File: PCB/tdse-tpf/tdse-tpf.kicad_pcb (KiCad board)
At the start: 2 copper layers, 100 x 100 mm, 11 parts, among them J1 CN7, J2 CN10, J3 Conn_01x04, J4 Conn_01x05, J5 Conn_01x02, J6 Conn_01x16, J7 Conn_01x04

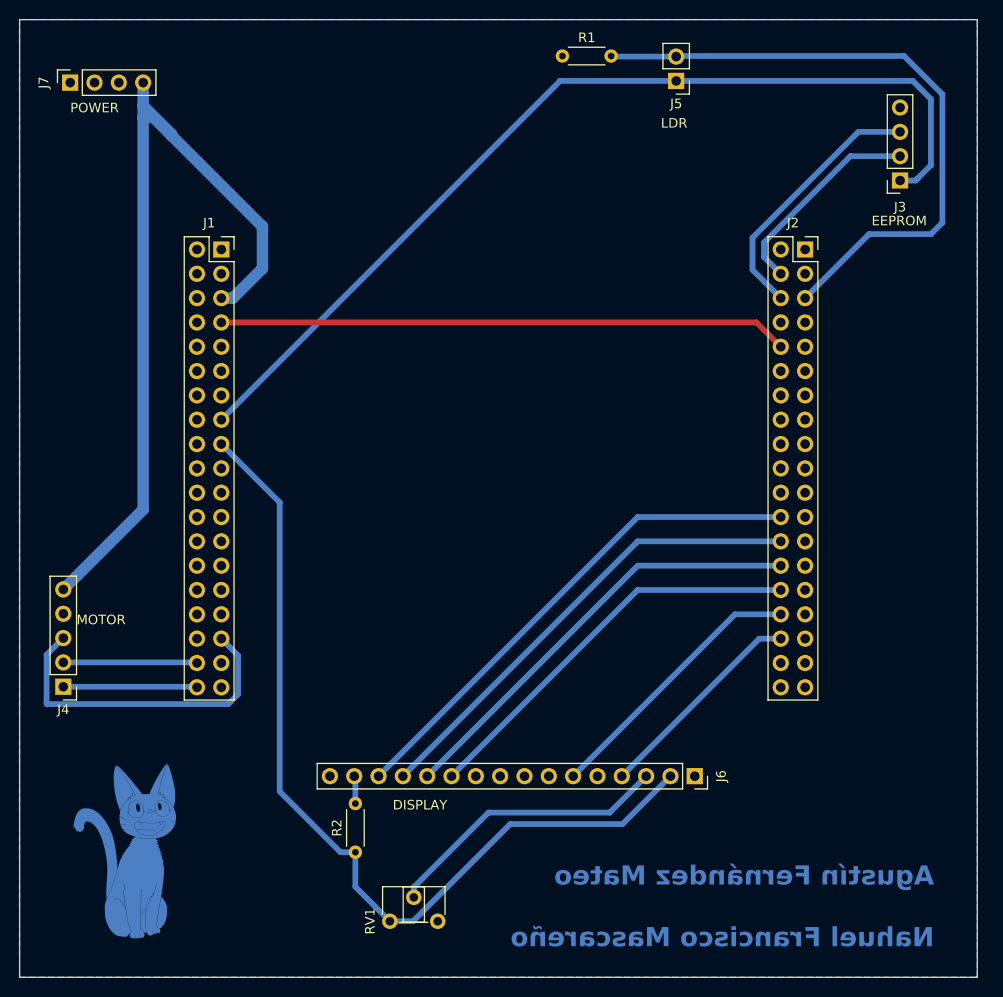
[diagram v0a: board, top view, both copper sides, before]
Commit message: Changed pins sensor-ldr-display & updated pcb pads
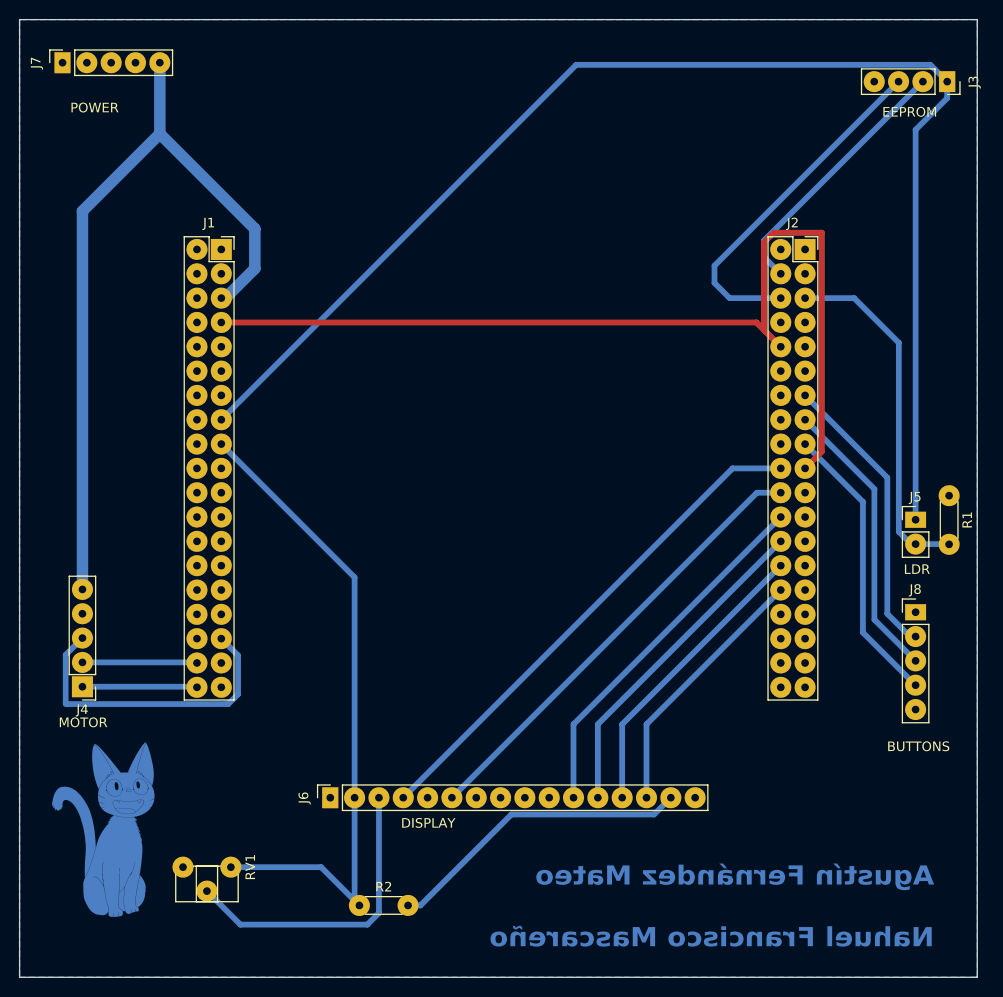
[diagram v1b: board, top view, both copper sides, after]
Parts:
- added J8: Conn_01x05, Connector_PinHeader_2.54mm:PinHeader_1x05_P2.54mm_Vertical, F.Cu at (180.0, 99.9)
- J7: value Conn_01x04 -> Conn_01x05; footprint Connector_PinSocket_2.54mm:PinSocket_1x04_P2.54mm_Vertical -> Connector_PinSocket_2.54mm:PinSocket_1x05_P2.54mm_Vertical
- moved R1 61.1 mm to (183.5, 87.7), turned to -90 degrees
- moved J5 52.2 mm to (180.0, 90.2), turned to 0 degrees
- moved J6 38.1 mm to (118.9, 119.2), turned to 90 degrees
- moved RV1 17.5 mm to (108.5, 126.5), turned to -90 degrees
- moved J3 11.4 mm to (183.3, 44.5), turned to -90 degrees
- moved R2 5.58 mm to (121.9, 130.5), turned to 0 degrees
- moved G*** 3.18 mm to (96.8, 122.8)
- moved J7 2.22 mm to (90.9, 42.5)
- moved J4 2.00 mm to (93.0, 107.7)
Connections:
- J2 pad 13: unconnected-(J2-Pin_13-Pad13) -> /ENT
- J2 pad 15: unconnected-(J2-Pin_15-Pad15) -> /NEX
- J2 pad 17: unconnected-(J2-Pin_17-Pad17) -> /ESC
- J2 pad 20: unconnected-(J2-Pin_20-Pad20) -> /RS
- J2 pad 22: unconnected-(J2-Pin_22-Pad22) -> /E
- J2 pad 24: /D7 -> /D4
- J2 pad 26: /D6 -> /D5
- J2 pad 28: /D5 -> /D6
- J2 pad 30: /D4 -> /D7
- J2 pad 32: /E -> unconnected-(J2-Pin_32-Pad32)
- J2 pad 34: /RS -> unconnected-(J2-Pin_34-Pad34)
- J7 pad 4: /E5V -> unconnected-(J7-Pin_4-Pad4)
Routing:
- net GND: track 59.5 -> 102.9 mm
- net +3V3: track 100.3 -> 139.0 mm
- net /RS: track 22.5 -> 53.7 mm
- net /ESC: track 0.00 -> 30.0 mm
- net /NEX: track 0.00 -> 30.0 mm
- net /PC5: track 67.3 -> 37.4 mm
- net /ENT: track 0.00 -> 29.7 mm
- net Net-(J6-Pin_15): track 3.08 -> 32.1 mm
- net /D7: track 53.2 -> 27.5 mm
- net +5V: track 93.6 -> 69.8 mm
- net /E: track 28.7 -> 47.5 mm
- net /D6: track 49.6 -> 31.1 mm
- net /D5: track 46.0 -> 34.7 mm
- net /SDA: track 27.5 -> 36.6 mm
- net /E5V: track 87.9 -> 81.3 mm
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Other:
- board text added: "${REFERENCE}"
- board text added: "BUTTONS"
